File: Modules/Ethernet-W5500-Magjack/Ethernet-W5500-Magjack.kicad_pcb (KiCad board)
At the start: 4 copper layers, 0 parts

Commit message: Prepare eight module boards and import their footprints
Set up the eight remaining layout blocks to the pattern of the PoE block.
Every board now holds its footprints, net classes and design rules. No
placement or routing yet.

Module projects
- Seven new projects under Modules/, from the Ethernet stub
- Each .kicad_pro binds its nets to classes. RF adds RF_50 (0.17 mm) on
  /ANT_433. USB boards add a USB pair class
- Each .kicad_dru carries the shared PCBWay rules. RF and PowerMux add a
  fanout rule. RF adds a J3 edge rule
- Update PCB from Schematic ran on all eight. check_import.py passes on
  each: same references, every class bound, the DRC canary fires

Schematic changes, each checked by a netlist membership diff
- Interface local labels are now hierarchical labels: V5_SYS, LED_*,
  USB_DP, USB_DM
- PowerMux R70 118k to 169k. PR1 reference is 1.06 V (SLVSEA3F), so the
  handover moves from 3.51 V to 4.57 V, as the note states
- Buck C100 10 uF 0805 to 22 uF 1206. The note names the TPS563208
- RF C22, C23, C29 value labels match their part numbers. U4 uses the
  stock footprint with no vias. Layout adds the 5 tented vias
- Title blocks name each block

Library policy: global rows only
- Remove the vendored PoEEthModule.pretty and every project library row.
  PoE DRC holds at 36 warnings and 0 library issues

Tooling
- check_courtyards.py and check_plan.py work on any board. 16 tests
- check_import.py, the acceptance test for GUI batch 1
- docs/Layout-Batch-Runbook.md
- A draft Layout-Spec.md for each new module

Co-Authored-By: Claude Opus 5.5 (1M context) <noreply@anthropic.com>
Claude-Session: https://claude.ai/code/session_01ErAAfkmF4h3T5yfrw21utF
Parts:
- added C50: 100nF, Capacitor_SMD:C_0603_1608Metric, F.Cu at (1.50, 23.4)
- added C51: 100nF, Capacitor_SMD:C_0603_1608Metric, F.Cu at (1.50, 25.9)
- added C52: 100nF, Capacitor_SMD:C_0603_1608Metric, F.Cu at (1.50, 28.4)
- added C53: 100nF, Capacitor_SMD:C_0603_1608Metric, F.Cu at (1.50, 30.9)
- added C54: 100nF, Capacitor_SMD:C_0603_1608Metric, F.Cu at (1.50, 33.4)
- added C55: 100nF, Capacitor_SMD:C_0603_1608Metric, F.Cu at (1.50, 35.9)
- added C56: 10uF 16V, Capacitor_SMD:C_0805_2012Metric, F.Cu at (22.0, 1.00)
- added C57: 100nF, Capacitor_SMD:C_0603_1608Metric, F.Cu at (5.51, 23.4)
- added C58: 10uF 16V, Capacitor_SMD:C_0805_2012Metric, F.Cu at (22.0, 4.01)
- added C59: 4.7uF, Capacitor_SMD:C_0805_2012Metric, F.Cu at (22.0, 7.03)
- added C60: 10nF, Capacitor_SMD:C_0603_1608Metric, F.Cu at (5.51, 25.9)
- added C61: 18pF NP0, Capacitor_SMD:C_0603_1608Metric, F.Cu at (5.51, 28.4)
- added C62: 18pF NP0, Capacitor_SMD:C_0603_1608Metric, F.Cu at (5.51, 30.9)
- added C63: 22nF, Capacitor_SMD:C_0603_1608Metric, F.Cu at (5.51, 33.4)
- added C64: 6.8nF, Capacitor_SMD:C_0603_1608Metric, F.Cu at (5.51, 35.9)
- added C65: 6.8nF, Capacitor_SMD:C_0603_1608Metric, F.Cu at (9.53, 23.4)
- added C66: 10nF, Capacitor_SMD:C_0603_1608Metric, F.Cu at (9.53, 25.9)
- added C67: 1nF 2kV, Capacitor_SMD:C_1808_4520Metric, F.Cu at (23.4, 10.5)
- added FB2: 120R@100MHz, Inductor_SMD:L_0603_1608Metric, F.Cu at (9.53, 28.4)
- added J2: ARJM11C7-114-BA-EW2, PlumRFBridge:RJ45_Abracon_ARJM11C7-114-BA-EW2, F.Cu at (9.55, 4.04)
- added R30: 12.4k 1%, Resistor_SMD:R_0603_1608Metric, F.Cu at (9.53, 30.9)
- added R31: 1M, Resistor_SMD:R_0603_1608Metric, F.Cu at (9.53, 33.4)
- added R32: 0R, Resistor_SMD:R_0603_1608Metric, F.Cu at (9.53, 35.9)
- added R33: 49R9 1%, Resistor_SMD:R_0603_1608Metric, F.Cu at (13.5, 23.4)
- added R34: 49R9 1%, Resistor_SMD:R_0603_1608Metric, F.Cu at (13.5, 25.9)
- added R35: 10R 1%, Resistor_SMD:R_0603_1608Metric, F.Cu at (13.5, 28.4)
- added R36: 49R9 1%, Resistor_SMD:R_0603_1608Metric, F.Cu at (13.5, 30.9)
- added R37: 49R9 1%, Resistor_SMD:R_0603_1608Metric, F.Cu at (13.5, 33.4)
- added R38: 330R, Resistor_SMD:R_0603_1608Metric, F.Cu at (13.5, 35.9)
- added R39: 330R, Resistor_SMD:R_0603_1608Metric, F.Cu at (17.5, 23.4)
- added R40: 4.7k, Resistor_SMD:R_0603_1608Metric, F.Cu at (17.5, 25.9)
- added R44: 0R, Resistor_SMD:R_0603_1608Metric, F.Cu at (17.5, 28.4)
- added R45: 0R, Resistor_SMD:R_0603_1608Metric, F.Cu at (17.5, 30.9)
- added R46: 0R, Resistor_SMD:R_0603_1608Metric, F.Cu at (17.5, 33.4)
- added R47: 0R, Resistor_SMD:R_0603_1608Metric, F.Cu at (17.5, 35.9)
- added U3: W5500, Package_QFP:LQFP-48_7x7mm_P0.5mm, F.Cu at (25.2, 27.8)
- added Y1: 25.000MHz CL=12pF, Crystal:Crystal_SMD_3225-4Pin_3.2x2.5mm, F.Cu at (22.4, 14.7)

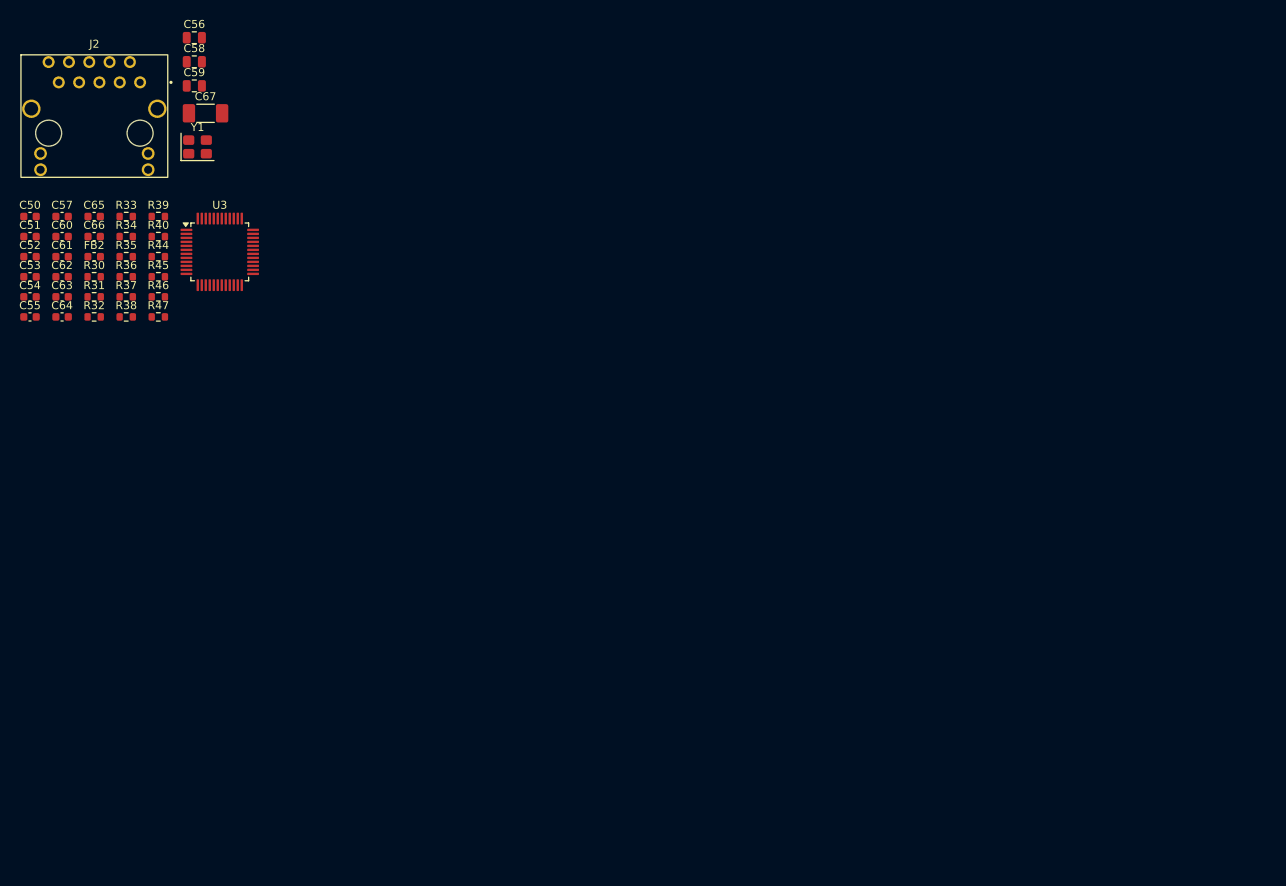
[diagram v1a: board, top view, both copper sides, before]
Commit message: Place and route the Ethernet module from the PoE copper
Place all 37 parts at the coordinates of their PoE module counterparts,
matched by the net on every pin. Replay 207 segments and 57 vias, then add
the line-side lanes, the SPI jog and the breakout row: 35 segments, 15 vias.

Rules: remove the MDI skew rule, which cannot pass across series parts.
Stop the line-side rule at J2's courtyard, as the PoE barrier stops at J1's.
Allow 0.35 mm hole to hole under U3 for the SPI fanout. DRC shows 0 errors,
and the canary rises from 69 to 568. Zones are not drawn yet.

Co-Authored-By: Claude Opus 5.5 (1M context) <noreply@anthropic.com>
Claude-Session: https://claude.ai/code/session_01ErAAfkmF4h3T5yfrw21utF
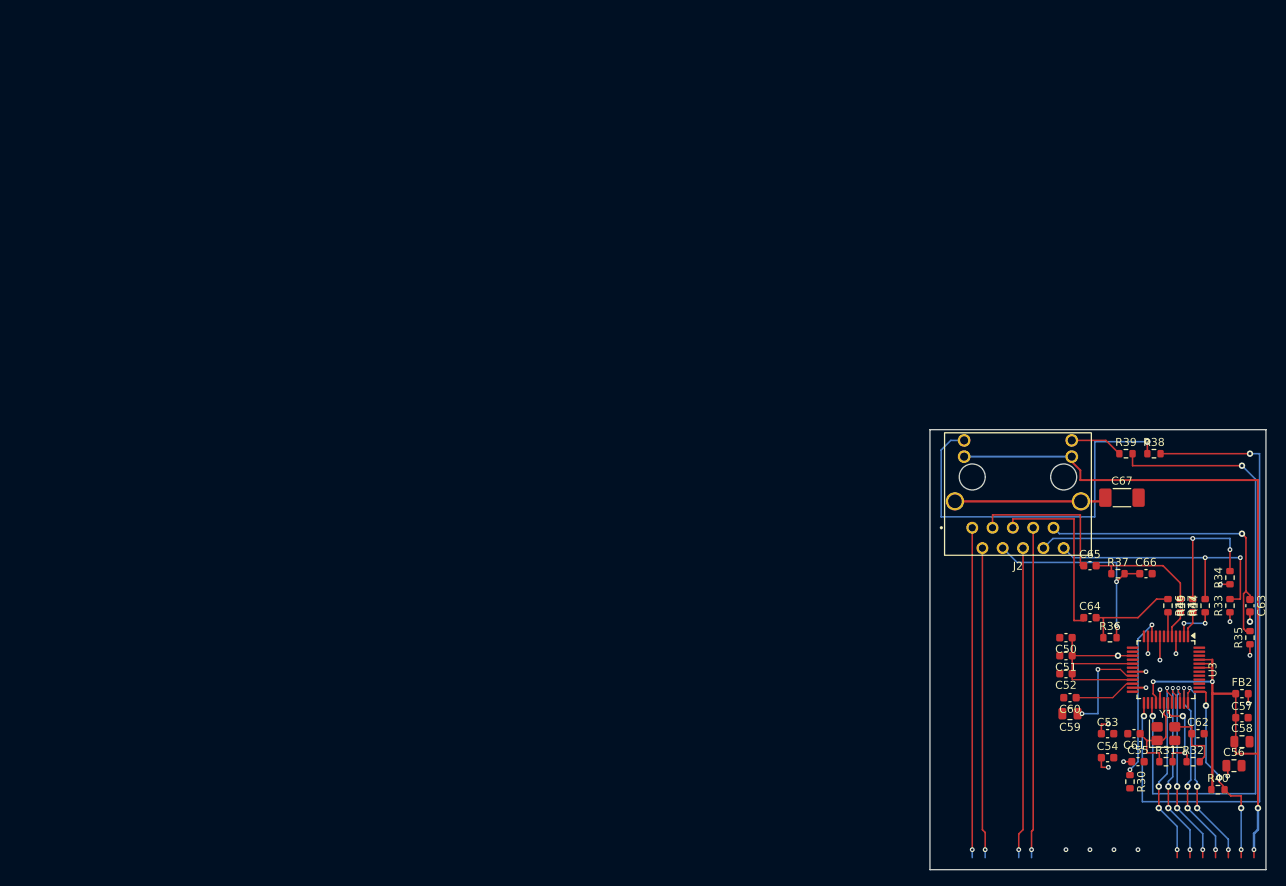
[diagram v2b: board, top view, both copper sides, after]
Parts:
- moved C57 160.2 mm to (153.0, 86.0)
- moved C56 158.6 mm to (152.0, 92.0)
- moved C58 156.1 mm to (153.0, 89.0)
- moved FB2 153.5 mm to (153.0, 83.0)
- moved C63 153.4 mm to (154.0, 72.0), turned to -90 degrees
- moved C62 153.0 mm to (147.5, 88.0)
- moved R40 149.4 mm to (150.0, 95.0)
- moved C55 149.2 mm to (140.0, 91.5)
- moved R35 148.3 mm to (154.0, 76.0), turned to 90 degrees
- moved R32 148.2 mm to (146.9, 91.5)
- moved C61 146.7 mm to (139.5, 88.0), turned to 180 degrees
- moved C54 146.5 mm to (136.2, 91.0)
- moved C53 146.3 mm to (136.2, 88.0)
- moved R33 146.3 mm to (151.5, 72.0), turned to 90 degrees
- moved R31 146.0 mm to (143.5, 91.5)
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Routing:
- net +3V3: track 0.00 -> 128.3 mm, vias 0 -> 4
- net /LINKLED: track 0.00 -> 82.6 mm, vias 0 -> 2
- net /ACTLED: track 0.00 -> 80.8 mm, vias 0 -> 2
- net /LED_LINK_K: track 0.00 -> 48.3 mm, vias 0 -> 1
- net /3V3A: track 0.00 -> 43.5 mm, vias 0 -> 12
- net /POE_VC1P: track 0.00 -> 41.3 mm, vias 0 -> 1
- net /POE_VC2N: track 0.00 -> 41.2 mm, vias 0 -> 1
- net /POE_VC2P: track 0.00 -> 38.9 mm, vias 0 -> 1
- net /POE_VC1N: track 0.00 -> 38.8 mm, vias 0 -> 1
- net /TCT: track 0.00 -> 38.2 mm, vias 0 -> 1
- net /TXN_MDI: track 0.00 -> 35.5 mm, vias 0 -> 2
- net /TXP_MDI: track 0.00 -> 34.2 mm, vias 0 -> 2
- net /RCT: track 0.00 -> 27.2 mm, vias 0 -> 2
- net /ETH_INT: track 0.00 -> 25.3 mm, vias 0 -> 4
- net /ETH_MOSI: track 0.00 -> 25.2 mm, vias 0 -> 4
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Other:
- board outline added: 42 x 55 mm

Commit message: Add the Ethernet zones and breakout labels
Five zones with the PoE module settings, cut to the 42 x 55 mm board: GND on
F.Cu, B.Cu and In1, the /3V3A island and the GND strip on In2. Fifteen F.Fab
labels on the breakout row.

DRC: 0 errors, 0 unconnected, 0 parity. The 11 track_dangling warnings are the
11 interface stubs. Silkscreen warnings wait for the silk pass.

Co-Authored-By: Claude Opus 5.5 (1M context) <noreply@anthropic.com>
Claude-Session: https://claude.ai/code/session_01ErAAfkmF4h3T5yfrw21utF
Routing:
- added copper zone on In2.Cu, net /3V3A
- added copper zone on B.Cu, net GND
- added copper zone on F.Cu, net GND
- added copper zone on In1.Cu, net GND
- added copper zone on In2.Cu, net GND
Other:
- board text added: "+3V3"
- board text added: "ETH_CLK"
- board text added: "ETH_CS"
- board text added: "ETH_INT"
- board text added: "ETH_MISO"
- board text added: "ETH_MOSI"
- board text added: "ETH_RST"
- board text added: "GND"
- board text added: "POE_VC1N"
- board text added: "POE_VC1P"
- board text added: "POE_VC2N"
- board text added: "POE_VC2P"
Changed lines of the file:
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@@
 	)
 	(embedded_fonts no)
-)
+  (zone (net 0) (net_name "GND") (layer "F.Cu")
+    (hatch edge 0.508)
+    (connect_pads (clearance 0.2))
+    (min_thickness 0.25)
+    (fill yes)
+    (polygon (pts
+      (xy 129.5 50.5)
+      (xy 155.5 50.5)
+      (xy 155.5 104.5)
+      (xy 129.5 104.5)
+    ))
+  )
+  (zone (net 0) (net_name "GND") (layer "B.Cu")
+    (hatch edge 0.508)
+    (connect_pads (clearance 0.2))
+    (min_thickness 0.25)
+    (fill yes)
+    (polygon (pts
+      (xy 129.5 50.5)
+      (xy 155.5 50.5)
+      (xy 155.5 104.5)
+      (xy 129.5 104.5)
+    ))
+  )
+  (zone (net 0) (net_name "GND") (layer "In1.Cu")
+    (hatch edge 0.508)
+    (connect_pads (clearance 0.2))
+    (min_thickness 0.25)
+    (fill yes)
+    (polygon (pts
+      (xy 129.5 50.5)
+      (xy 155.5 50.5)
+      (xy 155.5 104.5)
+      (xy 129.5 104.5)
+    ))
+  )
+  (zone (net 0) (net_name "GND") (layer "In2.Cu")
+    (hatch edge 0.508)
+    (connect_pads (clearance 0.2))
+    (min_thickness 0.25)
+    (fill yes)
+    (polygon (pts
+      (xy 129.5 95)
+      (xy 155.5 95)
+      (xy 155.5 104.5)
+      (xy 129.5 104.5)
+    ))
+  )
+  (zone (net 0) (net_name "/3V3A") (layer "In2.Cu")
+    (hatch edge 0.508)
+    (connect_pads (clearance 0.2))
+    (min_thickness 0.25)
+    (fill yes)
+    (polygon (pts
+      (xy 136 68)
+      (xy 155 68)
+      (xy 155 94)
+      (xy 136 94)
+    ))
+  )
+  (gr_text "GND"
+    (at 131 101.3 90)
+    (layer "F.Fab")
+    (effects (font (size 0.7 0.7) (thickness 0.15)))
+  )
+  (gr_text "GND"
+    (at 134 101.3 90)
+    (layer "F.Fab")
+    (effects (font (size 0.7 0.7) (thickness 0.15)))
+  )
+  (gr_text "GND"
+    (at 137 101.3 90)
+    (layer "F.Fab")
+    (effects (font (size 0.7 0.7) (thickness 0.15)))
+  )
+  (gr_text "GND"
+    (at 140 101.3 90)
+    (layer "F.Fab")
+    (effects (font (size 0.7 0.7) (thickness 0.15)))
+  )
+  (gr_text "ETH_CS"
+    (at 144.9 101.3 90)
+    (layer "F.Fab")
+    (effects (font (size 0.7 0.7) (thickness 0.15)))
+  )
+  (gr_text "ETH_CLK"
+    (at 146.5 101.3 90)
+    (layer "F.Fab")
+    (effects (font (size 0.7 0.7) (thickness 0.15)))
+  )
+  (gr_text "ETH_MISO"
+    (at 148.1 101.3 90)
+    (layer "F.Fab")
+    (effects (font (size 0.7 0.7) (thickness 0.15)))
+  )
+  (gr_text "ETH_MOSI"
+    (at 149.7 101.3 90)
+    (layer "F.Fab")
+    (effects (font (size 0.7 0.7) (thickness 0.15)))
+  )
+  (gr_text "ETH_INT"
+    (at 151.3 101.3 90)
+    (layer "F.Fab")
+    (effects (font (size 0.7 0.7) (thickness 0.15)))
+  )
+  (gr_text "ETH_RST"
+    (at 152.9 101.3 90)
+    (layer "F.Fab")
+    (effects (font (size 0.7 0.7) (thickness 0.15)))
+  )
+  (gr_text "+3V3"
+    (at 154.5 101.3 90)
+    (layer "F.Fab")
+    (effects (font (size 0.7 0.7) (thickness 0.15)))
+  )
+  (gr_text "POE_VC2N"
+    (at 119.285 101.3 90)
+    (layer "F.Fab")
+    (effects (font (size 0.7 0.7) (thickness 0.15)))
+  )
+  (gr_text "POE_VC1N"
+    (at 120.9 101.3 90)
+    (layer "F.Fab")
+    (effects (font (size 0.7 0.7) (thickness 0.15)))
+  )
+  (gr_text "POE_VC2P"
+    (at 125.1 101.3 90)
+    (layer "F.Fab")
+    (effects (font (size 0.7 0.7) (thickness 0.15)))
+  )
+  (gr_text "POE_VC1P"
+    (at 126.7 101.3 90)
+    (layer "F.Fab")
+    (effects (font (size 0.7 0.7) (thickness 0.15)))
+  ))

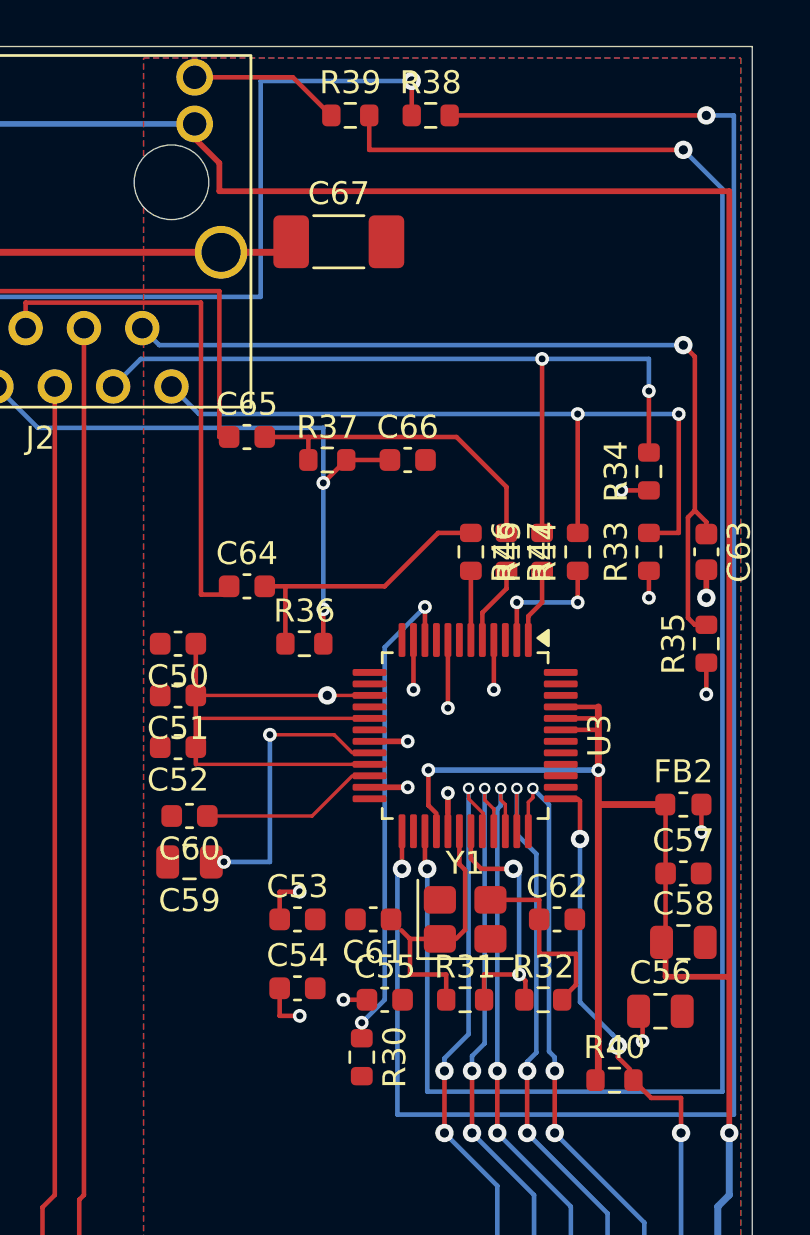
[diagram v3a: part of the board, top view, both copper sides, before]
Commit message: Restore footprints and move passive references to F.Fab
GUI batch 2a on all eight module boards. Update Footprints from Library
restores the (units) blocks that Konnect IPC writes dropped: U10, U1, SW1,
SW2 and U4 no longer report lib_footprint_mismatch. Reference designators of
C, R, L, FB, D, Y and TP parts move to F.Fab. U, J and SW stay on the silk.

Every board: DRC 0 errors, 0 unconnected, 0 parity, the canary fires, and
track_dangling equals the interface stub count.

Co-Authored-By: Claude Opus 5.5 (1M context) <noreply@anthropic.com>
Claude-Session: https://claude.ai/code/session_01ErAAfkmF4h3T5yfrw21utF
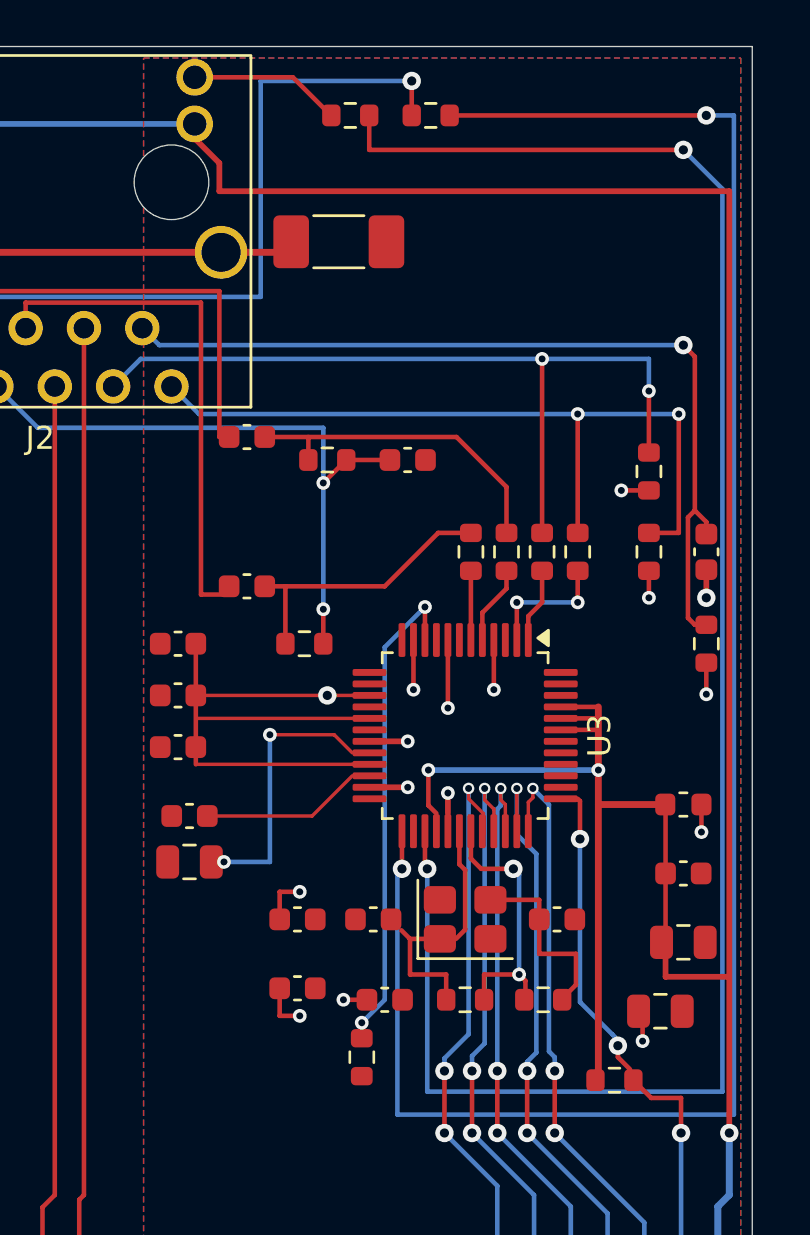
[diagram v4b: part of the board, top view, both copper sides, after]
